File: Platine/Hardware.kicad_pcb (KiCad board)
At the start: 2 copper layers, 245 x 250 mm, 164 parts, among them J1 Barrel_Jack_Switch, J2 Screw_Terminal_01x02, J3 USB_B, Q1 BCX19, Q2 BCX19, SW1 SW_Soft_Reset, SW2 SW_Hard_Reset, SW3 SW_Flash, U1 ESP32-WROOM-32D, U2 ZLDO1117_SOT223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

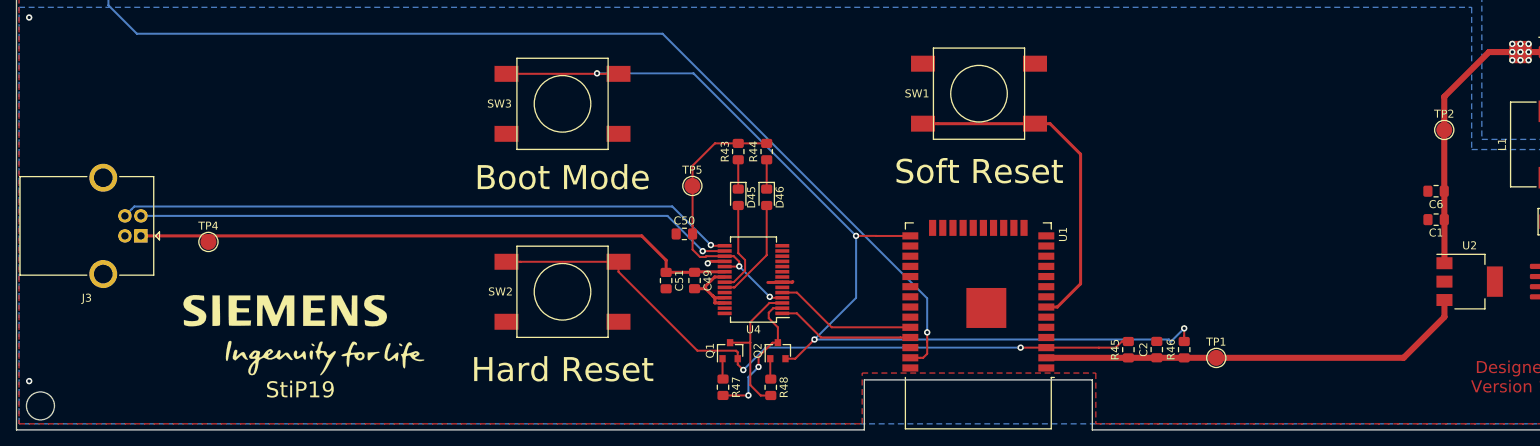
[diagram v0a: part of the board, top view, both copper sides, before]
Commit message: Added urgent features requested by client Added power LED Added option to supply complete PCB via USB port
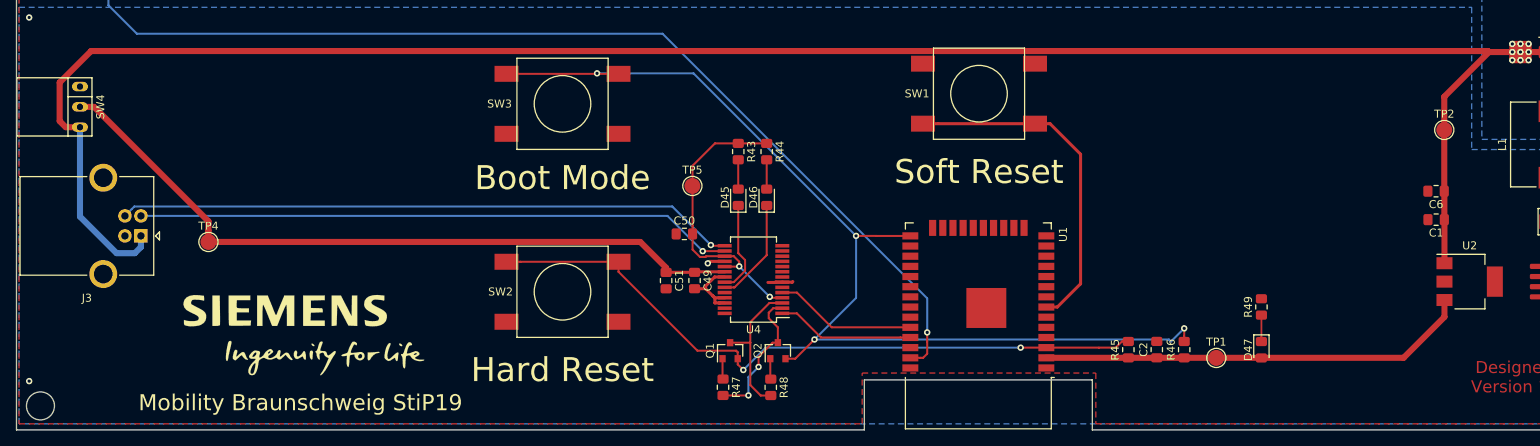
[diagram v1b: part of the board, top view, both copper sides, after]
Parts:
- added D47: LED, Diode_SMD:D_0805_2012Metric_Pad1.15x1.40mm_HandSolder, F.Cu at (175.6, 260.0)
- added R49: 300, Resistor_SMD:R_0805_2012Metric_Pad1.15x1.40mm_HandSolder, F.Cu at (175.6, 254.6)
- added SW4: SW_DPDT_x2, Custom_Footprints:Switch, F.Cu at (27.9, 229.6)
- turned D45 to 90 degrees
- turned D46 to 90 degrees
- turned R43 to 270 degrees
- turned R44 to 270 degrees
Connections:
- C1 pad 1: VCC -> V_USB
- C49 pad 1: V_USB -> V_FT232
- C5 pad 1: VCC -> V_USB
- C51 pad 1: V_USB -> V_FT232
- C6 pad 1: VCC -> V_USB
- D10 pad 5: VCC -> V_USB
- D11 pad 5: VCC -> V_USB
- D12 pad 5: VCC -> V_USB
- D13 pad 5: VCC -> V_USB
- D14 pad 5: VCC -> V_USB
- D15 pad 5: VCC -> V_USB
- D16 pad 5: VCC -> V_USB
- D17 pad 5: VCC -> V_USB
- D18 pad 5: VCC -> V_USB
- D19 pad 5: VCC -> V_USB
- D2 pad 5: VCC -> V_USB
- D20 pad 5: VCC -> V_USB
- D21 pad 5: VCC -> V_USB
- D22 pad 5: VCC -> V_USB
- D23 pad 5: VCC -> V_USB
- D24 pad 5: VCC -> V_USB
- D25 pad 5: VCC -> V_USB
- D26 pad 5: VCC -> V_USB
- D27 pad 5: VCC -> V_USB
- D28 pad 5: VCC -> V_USB
- D29 pad 5: VCC -> V_USB
- D3 pad 5: VCC -> V_USB
- D30 pad 5: VCC -> V_USB
- D31 pad 5: VCC -> V_USB
- D32 pad 5: VCC -> V_USB
- D33 pad 5: VCC -> V_USB
- D34 pad 5: VCC -> V_USB
- D35 pad 5: VCC -> V_USB
- D36 pad 5: VCC -> V_USB
- D37 pad 5: VCC -> V_USB
- D38 pad 5: VCC -> V_USB
- D39 pad 5: VCC -> V_USB
- D4 pad 5: VCC -> V_USB
- D40 pad 5: VCC -> V_USB
- D41 pad 5: VCC -> V_USB
- D42 pad 5: VCC -> V_USB
- D43 pad 5: VCC -> V_USB
- D5 pad 5: VCC -> V_USB
- D6 pad 5: VCC -> V_USB
- D7 pad 5: VCC -> V_USB
- D8 pad 5: VCC -> V_USB
- D9 pad 5: VCC -> V_USB
- L1 pad 2: VCC -> V_USB
- R1 pad 1: VCC -> V_USB
- R10 pad 1: VCC -> V_USB
- R11 pad 1: VCC -> V_USB
- R12 pad 1: VCC -> V_USB
- R13 pad 1: VCC -> V_USB
- R14 pad 1: VCC -> V_USB
- R15 pad 1: VCC -> V_USB
- R16 pad 1: VCC -> V_USB
- R17 pad 1: VCC -> V_USB
- R18 pad 1: VCC -> V_USB
- R19 pad 1: VCC -> V_USB
- R2 pad 1: VCC -> V_USB
- R20 pad 1: VCC -> V_USB
- R21 pad 1: VCC -> V_USB
- R22 pad 1: VCC -> V_USB
- R23 pad 1: VCC -> V_USB
- R24 pad 1: VCC -> V_USB
- R25 pad 1: VCC -> V_USB
- R26 pad 1: VCC -> V_USB
- R27 pad 1: VCC -> V_USB
- R28 pad 1: VCC -> V_USB
- R29 pad 1: VCC -> V_USB
- R3 pad 1: VCC -> V_USB
- R30 pad 1: VCC -> V_USB
- R31 pad 1: VCC -> V_USB
- R32 pad 1: VCC -> V_USB
- R33 pad 1: VCC -> V_USB
- R34 pad 1: VCC -> V_USB
- R35 pad 1: VCC -> V_USB
- R36 pad 1: VCC -> V_USB
- R37 pad 1: VCC -> V_USB
- R38 pad 1: VCC -> V_USB
- R39 pad 1: VCC -> V_USB
- R4 pad 1: VCC -> V_USB
- R40 pad 1: VCC -> V_USB
- R41 pad 1: VCC -> V_USB
- R42 pad 1: VCC -> V_USB
- R43 pad 1: Net-(D45-Pad1) -> V_FT_IO
- R43 pad 2: V_FT_IO -> Net-(D45-Pad2)
- R44 pad 1: Net-(D46-Pad1) -> V_FT_IO
- R44 pad 2: V_FT_IO -> Net-(D46-Pad2)
- R5 pad 1: VCC -> V_USB
- R6 pad 1: VCC -> V_USB
- R7 pad 1: VCC -> V_USB
- R8 pad 1: VCC -> V_USB
- R9 pad 1: VCC -> V_USB
- TP2 pad 1: VCC -> V_USB
- TP4 pad 1: V_USB -> V_FT232
- U1 pad 39: (no net) -> GND
- U2 pad 1: VCC -> V_USB
- U4 pad 20: V_USB -> V_FT232
- U4 pad 22: Net-(D45-Pad2) -> Net-(D45-Pad1)
- U4 pad 23: Net-(D46-Pad2) -> Net-(D46-Pad1)
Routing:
- net V_USB: track 76.9 -> 475.9 mm, vias 0 -> 93
- net VCC: track 265.4 -> 0.00 mm, vias 93 -> 0
- net V_FT232: track 0.00 -> 91.1 mm
- net Net-(D46-Pad2): track 13.1 -> 3.66 mm
- net Net-(D46-Pad1): track 3.66 -> 13.1 mm
- net Net-(D45-Pad2): track 11.7 -> 3.66 mm
- net Net-(D45-Pad1): track 3.66 -> 11.7 mm
- net Net-(D47-Pad1): track 0.00 -> 3.30 mm
- added copper zone on B.Cu, net V_USB
- removed copper zone on B.Cu, net VCC
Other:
- board text added: "Mobility Braunschweig StiP19"
- board text removed: "StiP19"

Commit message: Production readiness Improved reverse USB powerprotection Added part orderlist
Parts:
- added Q3: NDS0610, Package_TO_SOT_SMD:SOT-23, F.Cu at (185.2, 220.5)
- added R50: 10k, Resistor_SMD:R_0805_2012Metric_Pad1.15x1.40mm_HandSolder, F.Cu at (172.7, 238.5)
- added R51: 10k, Resistor_SMD:R_0805_2012Metric_Pad1.15x1.40mm_HandSolder, F.Cu at (172.7, 232.7)
- added U5: OP07, Package_SO:SO-8_5.3x6.2mm_P1.27mm, F.Cu at (185.2, 232.9)
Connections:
- net Net-(C3-Pad1) renamed V_IN
- C1 pad 1: V_USB -> VCC
- C5 pad 1: V_USB -> VCC
- C6 pad 1: V_USB -> VCC
- D10 pad 5: V_USB -> VCC
- D11 pad 5: V_USB -> VCC
- D12 pad 5: V_USB -> VCC
- D13 pad 5: V_USB -> VCC
- D14 pad 5: V_USB -> VCC
- D15 pad 5: V_USB -> VCC
- D16 pad 5: V_USB -> VCC
- D17 pad 5: V_USB -> VCC
- D18 pad 5: V_USB -> VCC
- D19 pad 5: V_USB -> VCC
- D2 pad 5: V_USB -> VCC
- D20 pad 5: V_USB -> VCC
- D21 pad 5: V_USB -> VCC
- D22 pad 5: V_USB -> VCC
- D23 pad 5: V_USB -> VCC
- D24 pad 5: V_USB -> VCC
- D25 pad 5: V_USB -> VCC
- D26 pad 5: V_USB -> VCC
- D27 pad 5: V_USB -> VCC
- D28 pad 5: V_USB -> VCC
- D29 pad 5: V_USB -> VCC
- D3 pad 5: V_USB -> VCC
- D30 pad 5: V_USB -> VCC
- D31 pad 5: V_USB -> VCC
- D32 pad 5: V_USB -> VCC
- D33 pad 5: V_USB -> VCC
- D34 pad 5: V_USB -> VCC
- D35 pad 5: V_USB -> VCC
- D36 pad 5: V_USB -> VCC
- D37 pad 5: V_USB -> VCC
- D38 pad 5: V_USB -> VCC
- D39 pad 5: V_USB -> VCC
- D4 pad 5: V_USB -> VCC
- D40 pad 5: V_USB -> VCC
- D41 pad 5: V_USB -> VCC
- D42 pad 5: V_USB -> VCC
- D43 pad 5: V_USB -> VCC
- D5 pad 5: V_USB -> VCC
- D6 pad 5: V_USB -> VCC
- D7 pad 5: V_USB -> VCC
- D8 pad 5: V_USB -> VCC
- D9 pad 5: V_USB -> VCC
- L1 pad 2: V_USB -> VCC
- R1 pad 1: V_USB -> VCC
- R10 pad 1: V_USB -> VCC
- R11 pad 1: V_USB -> VCC
- R12 pad 1: V_USB -> VCC
- R13 pad 1: V_USB -> VCC
- R14 pad 1: V_USB -> VCC
- R15 pad 1: V_USB -> VCC
- R16 pad 1: V_USB -> VCC
- R17 pad 1: V_USB -> VCC
- R18 pad 1: V_USB -> VCC
- R19 pad 1: V_USB -> VCC
- R2 pad 1: V_USB -> VCC
- R20 pad 1: V_USB -> VCC
- R21 pad 1: V_USB -> VCC
- R22 pad 1: V_USB -> VCC
- R23 pad 1: V_USB -> VCC
- R24 pad 1: V_USB -> VCC
- R25 pad 1: V_USB -> VCC
- R26 pad 1: V_USB -> VCC
- R27 pad 1: V_USB -> VCC
- R28 pad 1: V_USB -> VCC
- R29 pad 1: V_USB -> VCC
- R3 pad 1: V_USB -> VCC
- R30 pad 1: V_USB -> VCC
- R31 pad 1: V_USB -> VCC
- R32 pad 1: V_USB -> VCC
- R33 pad 1: V_USB -> VCC
- R34 pad 1: V_USB -> VCC
- R35 pad 1: V_USB -> VCC
- R36 pad 1: V_USB -> VCC
- R37 pad 1: V_USB -> VCC
- R38 pad 1: V_USB -> VCC
- R39 pad 1: V_USB -> VCC
- R4 pad 1: V_USB -> VCC
- R40 pad 1: V_USB -> VCC
- R41 pad 1: V_USB -> VCC
- R42 pad 1: V_USB -> VCC
- R5 pad 1: V_USB -> VCC
- R6 pad 1: V_USB -> VCC
- R7 pad 1: V_USB -> VCC
- R8 pad 1: V_USB -> VCC
- R9 pad 1: V_USB -> VCC
- TP2 pad 1: V_USB -> VCC
- U2 pad 1: V_USB -> VCC
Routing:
- net VCC: track 0.00 -> 293.8 mm, vias 0 -> 93
- net V_USB: track 475.9 -> 192.8 mm, vias 93 -> 0
- net V_IN: track 64.5 -> 128.5 mm, vias 0 -> 3
- net VCCQ: track 54.0 -> 85.7 mm
- net Net-(Q3-Pad1): track 0.00 -> 14.7 mm
- net Net-(R50-Pad2): track 0.00 -> 12.6 mm
- net Net-(J3-Pad3): vias 1 -> 2
- net GND: vias 5 -> 25
- added copper zone on B.Cu, net VCC
- removed copper zone on B.Cu, net V_USB

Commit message: Finished Layout V1 Created Gerber and Excellion drill files Updated BOM Added order manual Added orderlist Updated Schematic
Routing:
- net GND: vias 25 -> 64

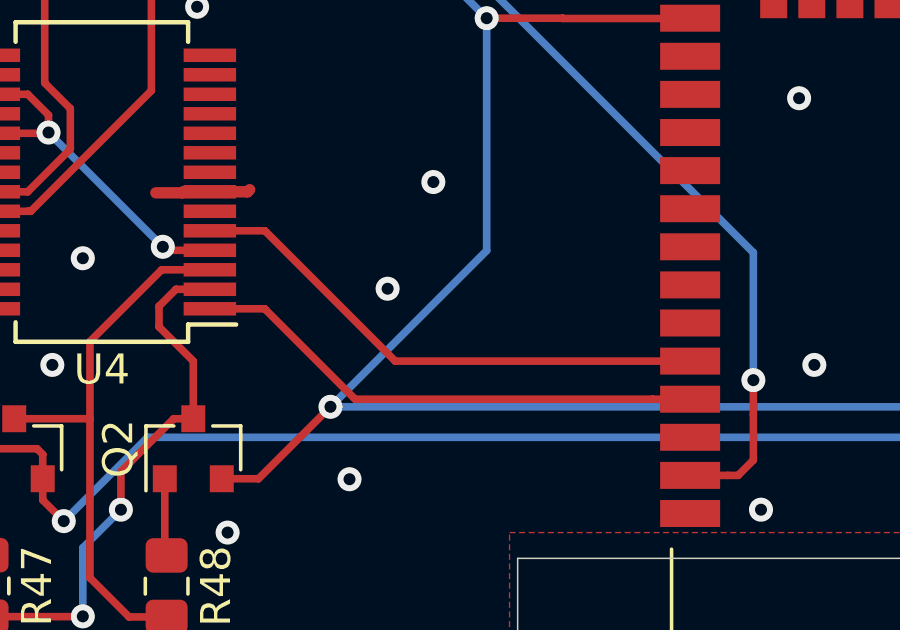
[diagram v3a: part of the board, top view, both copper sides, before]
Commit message: Fixed RX & TX Issue #5 Switched RX & TX of FT232RL and ESP 32.
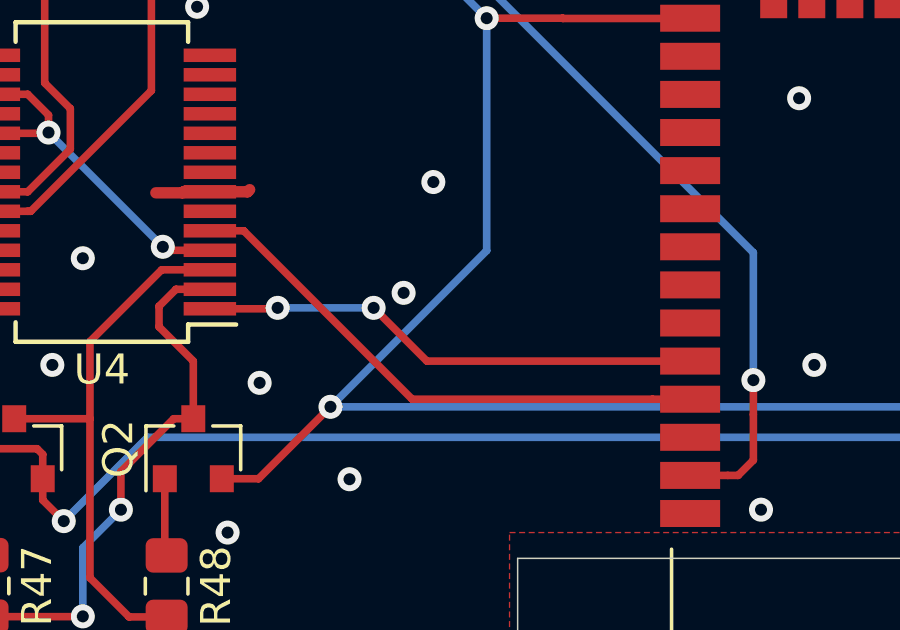
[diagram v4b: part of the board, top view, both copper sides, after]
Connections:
- U4 pad 1: RX0 -> TX0
- U4 pad 5: TX0 -> RX0
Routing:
- net RX0: track 17.3 -> 18.3 mm
- net TX0: track 17.8 -> 16.8 mm, vias 0 -> 2
- net GND: vias 64 -> 65

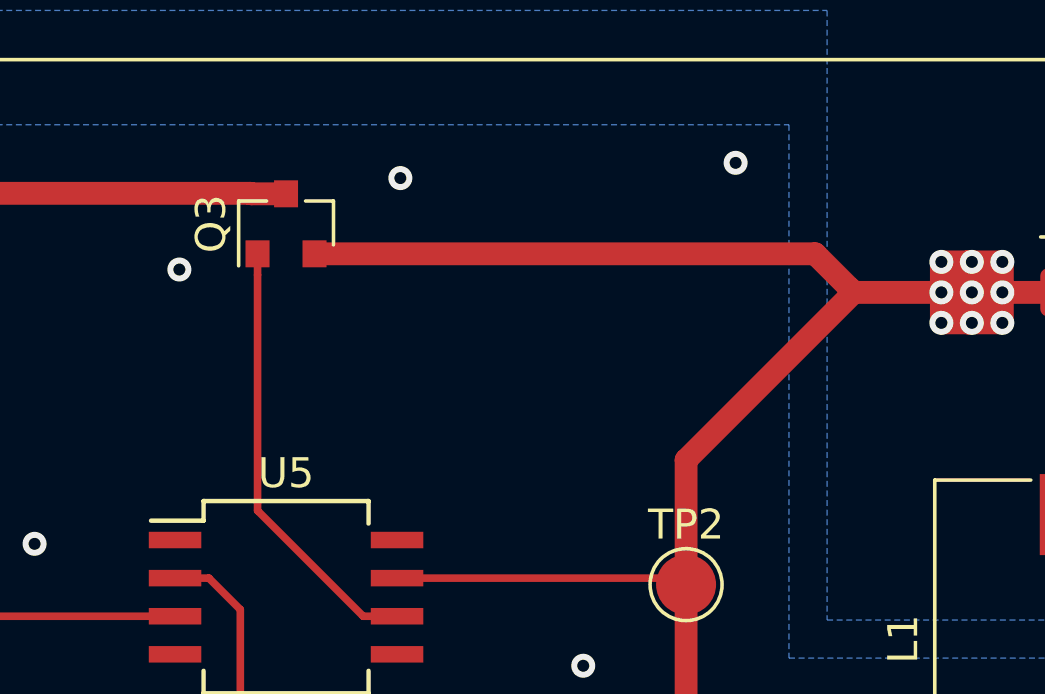
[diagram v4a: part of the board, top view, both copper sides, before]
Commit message: Resolved Issue 6 & Issue 7 Switched Pin 2 & 3 of P-FET (Issue 6) Upgraded P-FET to handle 2A continuous (Issue 7)
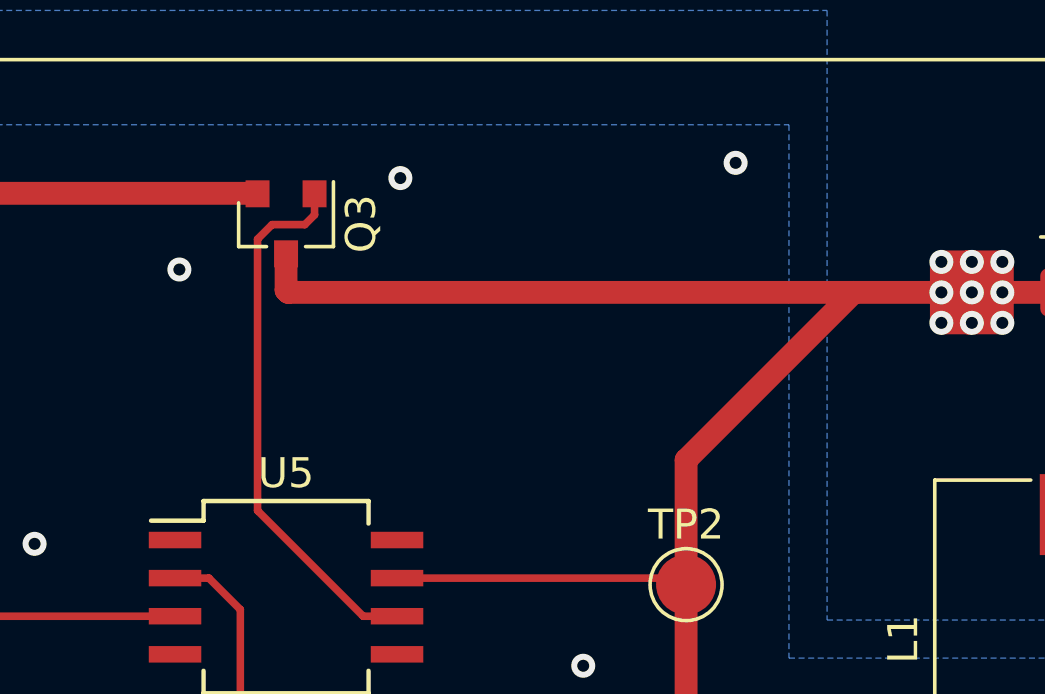
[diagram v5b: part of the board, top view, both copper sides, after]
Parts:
- Q3: value NDS0610 -> DMP3098L7
- turned Q3 to 270 degrees
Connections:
- Q3 pad 2: VCC -> V_USB
- Q3 pad 3: V_USB -> VCC
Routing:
- net Net-(Q3-Pad1): track 14.7 -> 18.1 mm
- net VCC: track 293.8 -> 295.3 mm
- net V_USB: track 192.8 -> 191.6 mm
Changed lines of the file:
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@@
     (thickness 1.6)
     (drawings 34)
-    (tracks 899)
+    (tracks 901)
     (zones 0)
     (modules 171)
@@
   )
   (setup
-    (last_trace_width 0.254)
+    (last_trace_width 0.762)
     (user_trace_width 0.2286)
     (user_trace_width 0.254)
@@
   )
   (module Package_TO_SOT_SMD:SOT-23 (layer F.Cu)
-    (at 185.166 220.472 90)
+    (at 185.166 220.472 270)
     (descr "SOT-23, Standard")
     (tags SOT-23)
@@
       (effects (font (size 1 1) (thickness 0.15)))
     )
-    (fp_text value NDS0610 (at 0 2.5 90) (layer F.Fab)
+    (fp_text value DMP3098L7 (at 0 2.5 90) (layer F.Fab)
       (effects (font (size 1 1) (thickness 0.15)))
     )
@@
       (effects (font (size 0.5 0.5) (thickness 0.075)))
     )
-    (pad 3 smd rect (at 1 0 90) (size 0.9 0.8) (layers F.Cu F.Paste F.Mask)
-      (net 173 V_USB))
-    (pad 2 smd rect (at -1 0.95 90) (size 0.9 0.8) (layers F.Cu F.Paste F.Mask)
+    (pad 3 smd rect (at 1 0 270) (size 0.9 0.8) (layers F.Cu F.Paste F.Mask)
       (net 189 VCC))
-    (pad 1 smd rect (at -1 -0.95 90) (size 0.9 0.8) (layers F.Cu F.Paste F.Mask)
+    (pad 2 smd rect (at -1 0.95 270) (size 0.9 0.8) (layers F.Cu F.Paste F.Mask)
+      (net 173 V_USB))
+    (pad 1 smd rect (at -1 -0.95 270) (size 0.9 0.8) (layers F.Cu F.Paste F.Mask)
       (net 191 "Net-(Q3-Pad1)"))
     (model ${KISYS3DMOD}/Package_TO_SOT_SMD.3dshapes/SOT-23.wrl
@@
   (segment (start 26.162 232.156) (end 27.94 232.156) (width 0.762) (layer F.Cu) (net 173))
   (segment (start 25.4 231.394) (end 26.162 232.156) (width 0.762) (layer F.Cu) (net 173))
-  (segment (start 185.166 219.472) (end 184.004 219.472) (width 0.762) (layer F.Cu) (net 173))
   (segment (start 184.004 219.472) (end 183.988 219.456) (width 0.762) (layer F.Cu) (net 173))
   (segment (start 183.988 219.456) (end 32.512 219.456) (width 0.762) (layer F.Cu) (net 173))
@@
   (segment (start 198.501 228.346) (end 204.089 222.758) (width 0.762) (layer F.Cu) (net 189))
   (segment (start 204.089 222.758) (end 207.01 222.758) (width 0.762) (layer F.Cu) (net 189))
-  (segment (start 203.964999 222.633999) (end 204.089 222.758) (width 0.762) (layer F.Cu) (net 189))
-  (segment (start 202.803 221.472) (end 204.089 222.758) (width 0.762) (layer F.Cu) (net 189))
-  (segment (start 186.116 221.472) (end 202.803 221.472) (width 0.762) (layer F.Cu) (net 189))
   (segment (start 198.283 232.283) (end 198.5 232.5) (width 0.254) (layer F.Cu) (net 189))
   (segment (start 188.866 232.283) (end 198.283 232.283) (width 0.254) (layer F.Cu) (net 189))
+  (segment (start 185.24 222.758) (end 185.166 222.684) (width 0.762) (layer F.Cu) (net 189))
+  (segment (start 185.166 222.684) (end 185.166 221.472) (width 0.762) (layer F.Cu) (net 189))
+  (segment (start 204.089 222.758) (end 185.24 222.758) (width 0.762) (layer F.Cu) (net 189))
   (segment (start 250.825 252.73) (end 242.61 252.73) (width 0.762) (layer F.Cu) (net 190))
   (segment (start 242.57 252.69) (end 231.975 252.69) (width 0.762) (layer F.Cu) (net 190))
@@
   (segment (start 194.564 255.27) (end 217.17 255.27) (width 0.254) (layer B.Cu) (net 190))
   (via (at 194.564 255.27) (size 0.8) (drill 0.4) (layers F.Cu B.Cu) (net 190))
-  (segment (start 184.216 222.176) (end 184.216 221.472) (width 0.254) (layer F.Cu) (net 191))
-  (segment (start 184.216 230.032) (end 184.216 222.176) (width 0.254) (layer F.Cu) (net 191))
-  (segment (start 187.737 233.553) (end 184.216 230.032) (width 0.254) (layer F.Cu) (net 191))
+  (segment (start 186.116 220.176) (end 186.116 219.472) (width 0.254) (layer F.Cu) (net 191))
   (segment (start 188.866 233.553) (end 187.737 233.553) (width 0.254) (layer F.Cu) (net 191))
+  (segment (start 187.737 233.553) (end 184.216 230.032) (width 0.254) (layer F.Cu) (net 191))
+  (segment (start 185.792 220.5) (end 186.116 220.176) (width 0.254) (layer F.Cu) (net 191))
+  (segment (start 184.216 230.032) (end 184.216 220.983398) (width 0.254) (layer F.Cu) (net 191))
+  (segment (start 184.699398 220.5) (end 185.792 220.5) (width 0.254) (layer F.Cu) (net 191))
+  (segment (start 184.216 220.983398) (end 184.699398 220.5) (width 0.254) (layer F.Cu) (net 191))
   (segment (start 172.856 233.553) (end 172.72 233.689) (width 0.254) (layer F.Cu) (net 192))
   (segment (start 181.466 233.553) (end 172.856 233.553) (width 0.254) (layer F.Cu) (net 192))
